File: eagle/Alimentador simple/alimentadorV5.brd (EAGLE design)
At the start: 74.9 x 44.5 mm, 33 parts, among them T1 AO3403, T2 AO3403, T3 AO3403, T4 AO3403, T5 AO3403

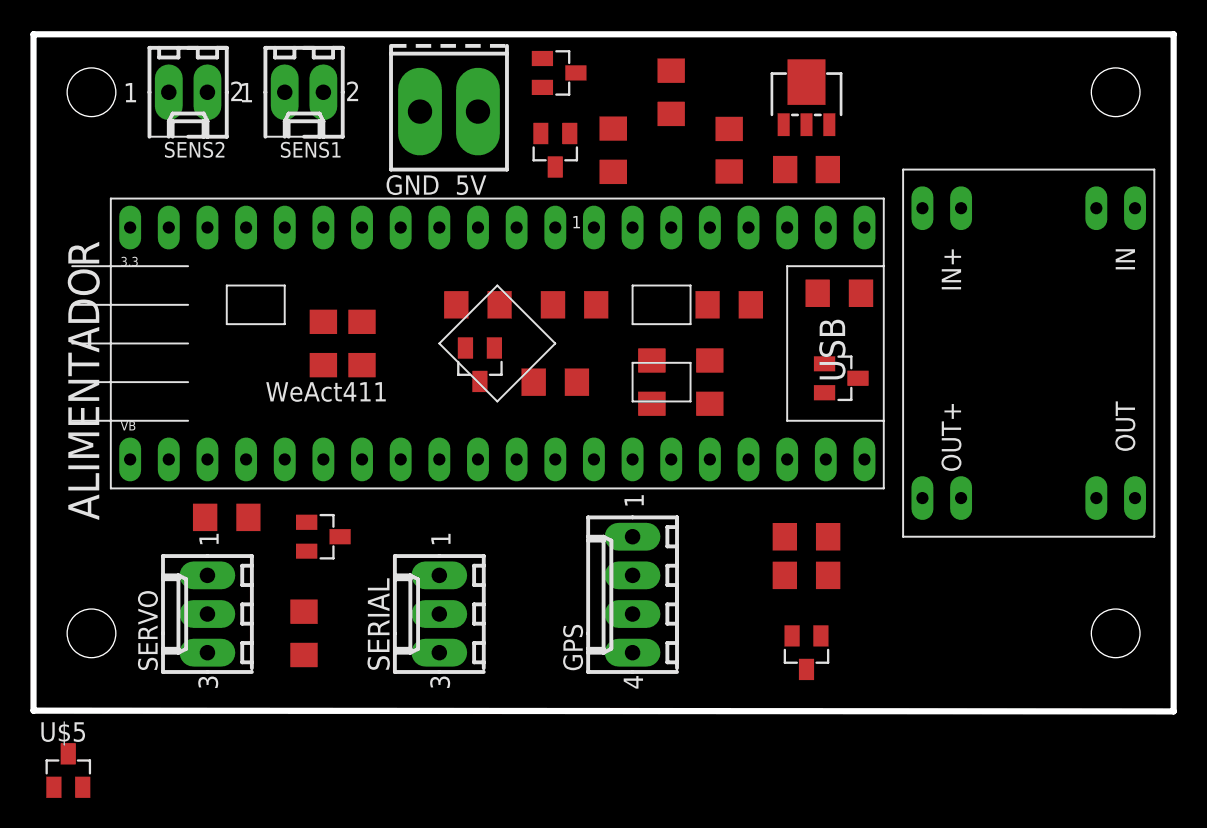
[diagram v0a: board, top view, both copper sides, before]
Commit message: Con posiciones de servo
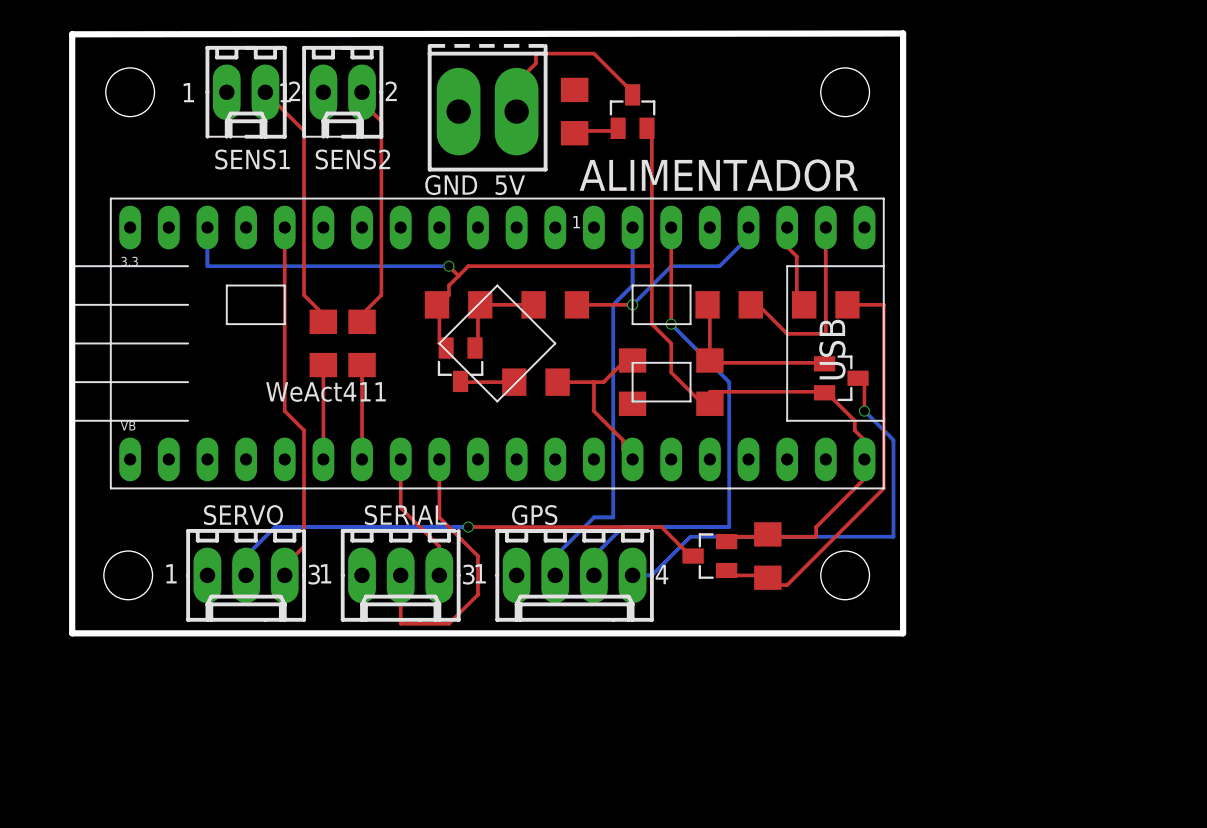
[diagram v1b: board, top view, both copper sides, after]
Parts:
- removed C2, C3: 100nF, rcl:C1206
- removed R10, R9: 220, rcl:R1206
- removed R15: 10k, rcl:R1206
- removed R8: 47k, rcl:R1206
- removed T5: AO3403, jcf:SOT23
- removed U$1: AO3400-NMOSFET, jcf:SOT23
- removed U$3: REG12TO5, jcf:REG12TO5
- removed U$4: HT7133, jcf:SOT89
- removed U$5: AO3400, jcf:SOT23
- R1, R11, R5: value 47k -> 500k
- moved R6 15.3 mm to (48.3, 25.4)
- moved SENS2 10.2 mm to (16.5, 39.4)
- moved T3 8.98 mm to (40.6, 8.89), turned to 90 degrees
- moved T4 5.68 mm to (35.6, 38.1), turned to 0 degrees
- moved GPS 4.02 mm to (31.8, 7.62), turned to 180 degrees
- moved SENS1 3.81 mm to (10.2, 39.4)
- moved SERVO 3.59 mm to (10.2, 7.62), turned to 180 degrees
- moved SERIAL 3.59 mm to (20.3, 7.62), turned to 180 degrees
- moved R7 3.59 mm to (31.8, 38.1), turned to 90 degrees
- moved R5 2.84 mm to (44.5, 8.89), turned to 90 degrees
- moved LIPO2S 2.54 mm to (24.1, 38.1)
- moved R11 1.27 mm to (24.1, 25.4)
- moved R12 1.27 mm to (30.5, 25.4)
- moved R3 1.27 mm to (29.2, 20.3)
- moved T1 1.27 mm to (24.3, 21.5)
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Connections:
- removed net 3V3: C3.1, U$2.3V3@1, U$2.3V3@2, U$4.2
- removed net KK: T5.3, U$3.IN+@1, U$3.IN+@2
- removed net N$4: R8.1, R9.2, T5.1
- removed net N$7: R10.1, R15.1, U$1.1
- removed net ON-5V: R10.2, U$2.B12
- removed net UU: R9.1, U$1.3
- removed net VCC: C2.1, R11.2, R8.2, T1.2, T4.2, T5.2, U$4.1
- net +5V: now also R11.2, T1.2, T4.2, U$2.5V@1, U$2.5V@2; no longer U$3.OUT+@1, U$3.OUT+@2
- net GND: no longer C2.2, C3.2, R15.2, U$1.2, U$3.GND@1, U$3.GND@2, U$3.GND@3, U$3.GND@4, U$4.3, U$4.4
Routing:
- net +5V: track 0.00 -> 85.3 mm, vias 0 -> 1
- net VCC-SERVO: track 0.00 -> 32.2 mm, vias 0 -> 1
- net TX1: track 0.00 -> 32.2 mm, vias 0 -> 1
- net VCC-GPS: track 0.00 -> 29.6 mm, vias 0 -> 1
- net N$8: track 0.00 -> 28.2 mm
- net RX1: track 0.00 -> 25.7 mm
- net B8-PWM: track 0.00 -> 23.9 mm
- net RX2: track 0.00 -> 19.0 mm
- net A0-SENS1: track 0.00 -> 16.7 mm
- net A1-SENS2: track 0.00 -> 16.1 mm
- net ON-AD: track 0.00 -> 13.8 mm, vias 0 -> 1
- net ON-GPS: track 0.00 -> 12.7 mm
- net N$2: track 0.00 -> 12.3 mm
- net N$1: track 0.00 -> 11.9 mm
- net N$5: track 0.00 -> 11.5 mm
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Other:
- board size 74.9 x 44.5 mm -> 54.6 x 39.4 mm
